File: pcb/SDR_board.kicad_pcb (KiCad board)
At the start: 4 copper layers, 100 x 100 mm, 463 parts, among them J1 USB_B_Mini, J201 Molex 73251-1150 SMA, J301 Molex 73251-1150 SMA, J401 Molex 73251-1150 SMA, J501 Molex 73251-1150 SMA, SW1 SW_Push, U1 AMS1117-3.3, U2 NB3L553, U201 BGA2803, U202 MSi001-Q40, U203 MAX19777AZA+, U204 ADS7883, U205 LMV712-N, U206 MAX19777AZA+, U207 ADS7883, U3 CY7C68013A-56PVX, U301 BGA2803, U302 MSi001-Q40, U303 MAX19777AZA+, U304 ADS7883, U305 LMV712-N, U306 MAX19777AZA+, U307 ADS7883, U401 BGA2803, U402 MSi001-Q40, U403 MAX19777AZA+, U404 ADS7883, U405 LMV712-N, U406 MAX19777AZA+, U407 ADS7883, U5 24LC128, U501 BGA2803, U502 MSi001-Q40, U503 MAX19777AZA+, U504 ADS7883, U505 LMV712-N, U506 MAX19777AZA+, U507 ADS7883, U6 MCP1825S, X1 XO32, X2 XO32

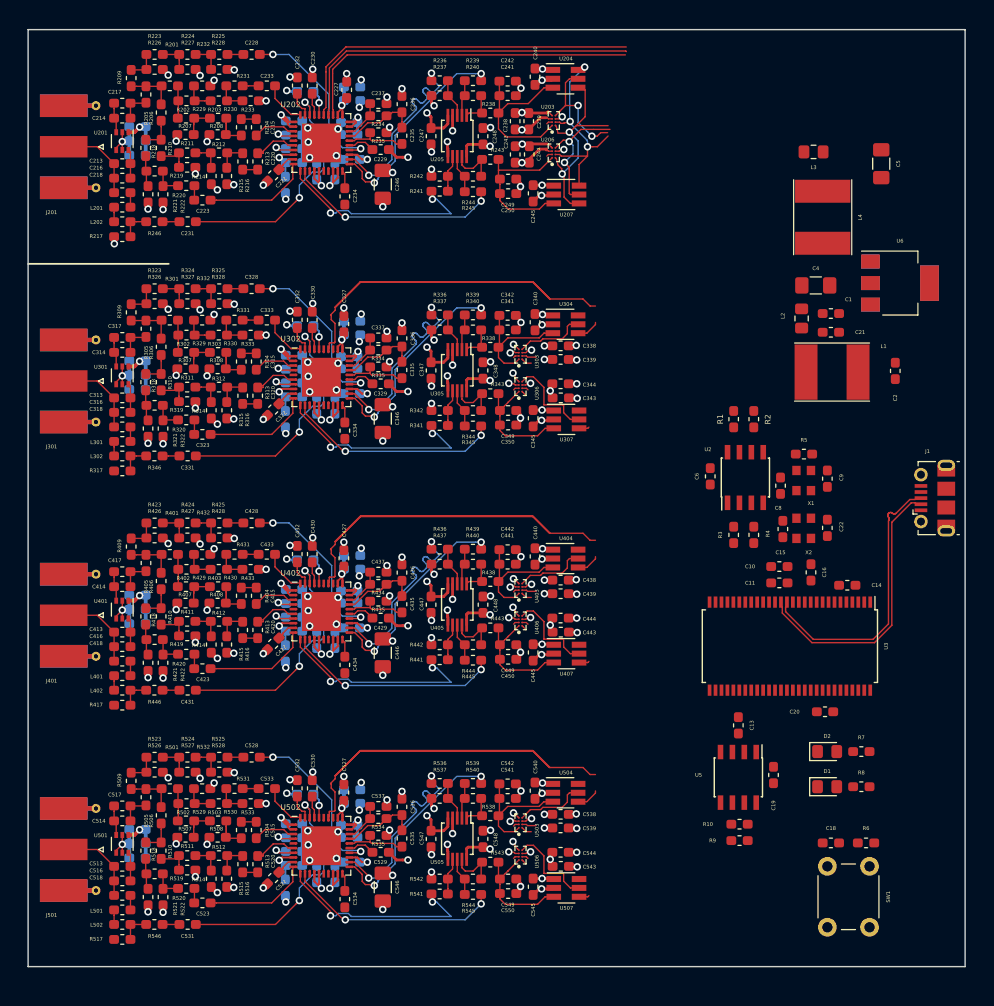
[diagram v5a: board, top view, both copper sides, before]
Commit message: Think the channels are done this time, for real
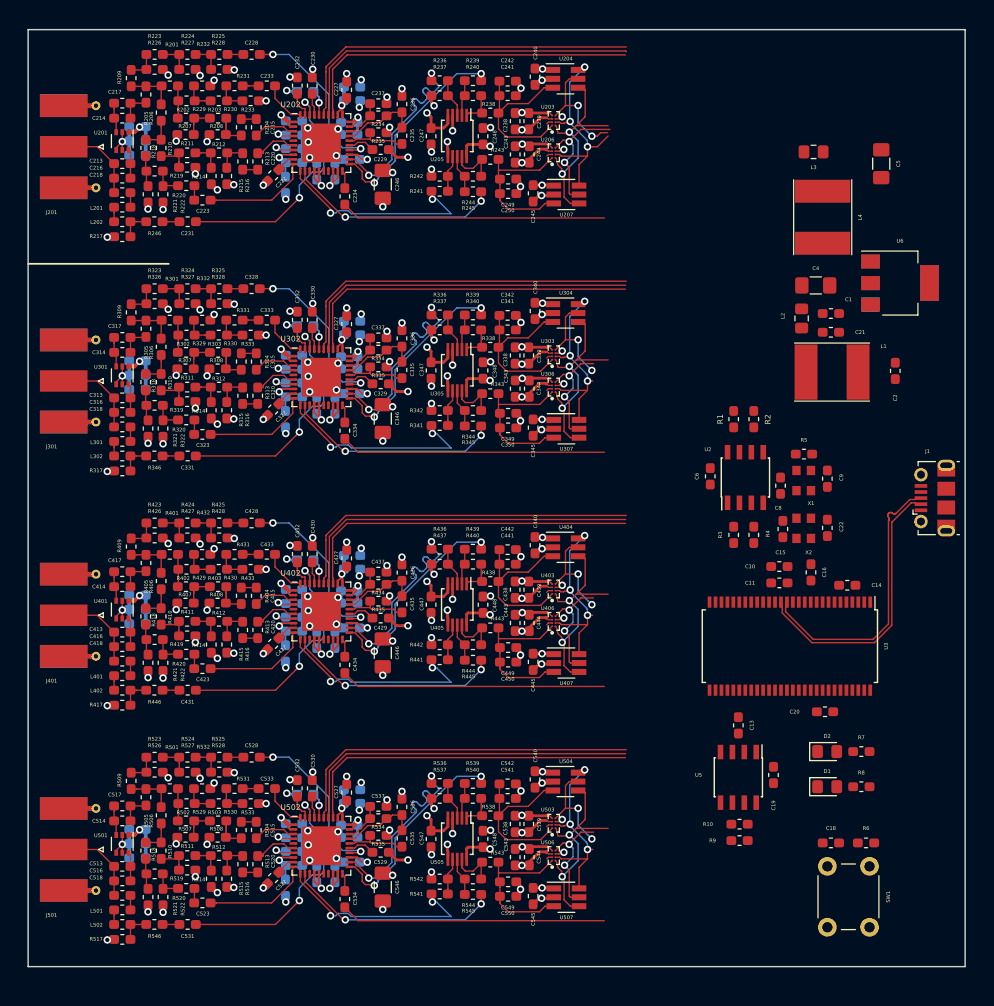
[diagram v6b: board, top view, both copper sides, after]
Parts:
- moved C343 4.96 mm to (77.0, 58.3), turned to 270 degrees
- moved C443 4.96 mm to (77.0, 83.3), turned to 270 degrees
- moved C543 4.96 mm to (77.0, 108.3), turned to 270 degrees
- moved C339 4.86 mm to (77.0, 54.8), turned to 90 degrees
- moved C439 4.86 mm to (77.0, 79.8), turned to 90 degrees
- moved C539 4.86 mm to (77.0, 104.8), turned to 90 degrees
- moved U303 3.55 mm to (81.1, 54.7)
- moved U306 3.55 mm to (81.1, 58.1)
- moved U403 3.55 mm to (81.1, 79.7)
- moved U406 3.55 mm to (81.1, 83.2)
- moved U503 3.55 mm to (81.1, 104.7)
- moved U506 3.55 mm to (81.1, 108.2)
- moved C438 3.55 mm to (78.4, 79.8), turned to 270 degrees
- moved C538 3.55 mm to (78.4, 104.8), turned to 270 degrees
- moved C338 3.55 mm to (78.4, 54.8), turned to 270 degrees
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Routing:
- net TUNER_SPI_CLK: track 366.4 -> 150.1 mm
- net TUNER_SPI_MOSI: track 38.1 -> 152.5 mm
- net ADC_nCS: track 30.6 -> 89.5 mm, vias 3 -> 12
- net ADC_CLK: track 42.0 -> 96.7 mm, vias 2 -> 8
- net /TUNER_4_nCS: track 0.00 -> 36.7 mm
- net /TUNER_3_nCS: track 0.00 -> 36.7 mm
- net /TUNER_2_nCS: track 0.00 -> 36.7 mm
- net /TUNER_1_CLK: track 0.00 -> 28.3 mm
- net /TUNER_4_CLK: track 0.00 -> 28.3 mm
- net /TUNER_3_CLK: track 0.00 -> 28.3 mm
- net /TUNER_2_CLK: track 0.00 -> 28.3 mm
- net GND: track 322.0 -> 336.3 mm, vias 189 -> 180
- net +3.3VA: track 205.2 -> 215.3 mm, vias 73 -> 64
- net /Channel 4/BUFFERED_SINGLE_Q: track 13.6 -> 18.6 mm
- net /Channel 3/BUFFERED_SINGLE_Q: track 13.6 -> 18.6 mm
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
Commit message: Board layout complete
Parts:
- added M3.2: MountingHole_3.2mm_M3_DIN965_Pad, Mounting_Holes:MountingHole_3.2mm_M3_DIN965_Pad, F.Cu at (121.0, 116.0)
- added M3.2: MountingHole_3.2mm_M3_DIN965_Pad, Mounting_Holes:MountingHole_3.2mm_M3_DIN965_Pad, F.Cu at (121.0, 24.0)
- added M3.2: MountingHole_3.2mm_M3_DIN965_Pad, Mounting_Holes:MountingHole_3.2mm_M3_DIN965_Pad, F.Cu at (29.0, 45.0)
- added M3.2: MountingHole_3.2mm_M3_DIN965_Pad, Mounting_Holes:MountingHole_3.2mm_M3_DIN965_Pad, F.Cu at (29.0, 95.0)
- U1: moved to F.Cu
- moved C5 11.8 mm to (107.4, 26.3), turned to 0 degrees
- moved U1 11.3 mm to (107.9, 42.0), turned to 90 degrees
- moved C2 9.79 mm to (118.4, 66.2), turned to 270 degrees
- moved C4 9.57 mm to (117.6, 51.6)
- moved C21 8.88 mm to (119.4, 54.1)
- moved L2 8.81 mm to (115.7, 54.1), turned to 0 degrees
- moved C1 8.54 mm to (112.7, 42.0), turned to 270 degrees
- moved L4 8.45 mm to (113.0, 32.2)
- moved L1 7.50 mm to (117.5, 59.9), turned to 270 degrees
- moved C18 6.52 mm to (116.8, 109.2), turned to 270 degrees
- moved SW1 5.60 mm to (113.5, 103.8)
- moved U6 5.03 mm to (117.5, 42.0), turned to 90 degrees
- moved L3 4.23 mm to (107.3, 29.1), turned to 0 degrees
- moved R6 2.70 mm to (116.8, 105.4), turned to 270 degrees
- moved D1 1.80 mm to (110.2, 99.0)
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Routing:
- net +3V3: track 20.9 -> 243.6 mm, vias 4 -> 26
- net TUNER_SPI_MOSI: track 152.5 -> 310.3 mm, vias 0 -> 7
- net TUNER_SPI_CLK: track 150.1 -> 295.5 mm, vias 0 -> 6
- net ADC_CLK: track 96.7 -> 221.2 mm, vias 8 -> 18
- net ADC_nCS: track 89.5 -> 212.3 mm, vias 12 -> 18
- net /TUNER_1_nCS: track 36.7 -> 117.1 mm, vias 0 -> 2
- net GND: track 336.3 -> 409.1 mm, vias 180 -> 201
- net /TUNER_2_nCS: track 36.7 -> 103.3 mm, vias 0 -> 4
- net /Channel 1/I_DOUT: track 14.3 -> 73.1 mm, vias 2 -> 4
- net /Channel 1/Q_DOUT: track 12.7 -> 70.2 mm, vias 2 -> 4
- net /TUNER_1_CLK: track 28.3 -> 79.4 mm
- net /TUNER_2_CLK: track 28.3 -> 79.3 mm
- net /TUNER_3_CLK: track 28.3 -> 78.9 mm
- net /TUNER_4_CLK: track 28.3 -> 78.4 mm
- net /TUNER_3_nCS: track 36.7 -> 75.7 mm, vias 0 -> 2
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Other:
- outline, holes or cut-outs redrawn
- net class Default: clearance 0.2 -> 0.18
- net class Power: clearance 0.2 -> 0.18
- rule trace_clearance: 0.2 -> 0.18
- board text added: "AMS"
- board text added: "CH1"
- board text added: "CH2"
- board text added: "CH3"
- board text added: "CH4"
- board text added: "I2C pullups"
- board text added: "MCP"
- board text added: "Reset"

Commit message: Silkscreening done
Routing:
- added copper zone on B.Cu, net GND
- added copper zone on F.Cu, net GND
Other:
- board text added: "4-Ch Narrowband SDR"
- board text added: "PA0"
- board text added: "PA1"
- board text added: "v0.1 (2020 FYP) William Woods"
